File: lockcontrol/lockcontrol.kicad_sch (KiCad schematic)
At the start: 8 parts, among them J1 ButtonHeader, K1 G5Q-1A, U1 WeMos_D1_mini, U3 ULN2003, U4 Barrel_Jack_Switch, U5 Barrel_Jack_Switch

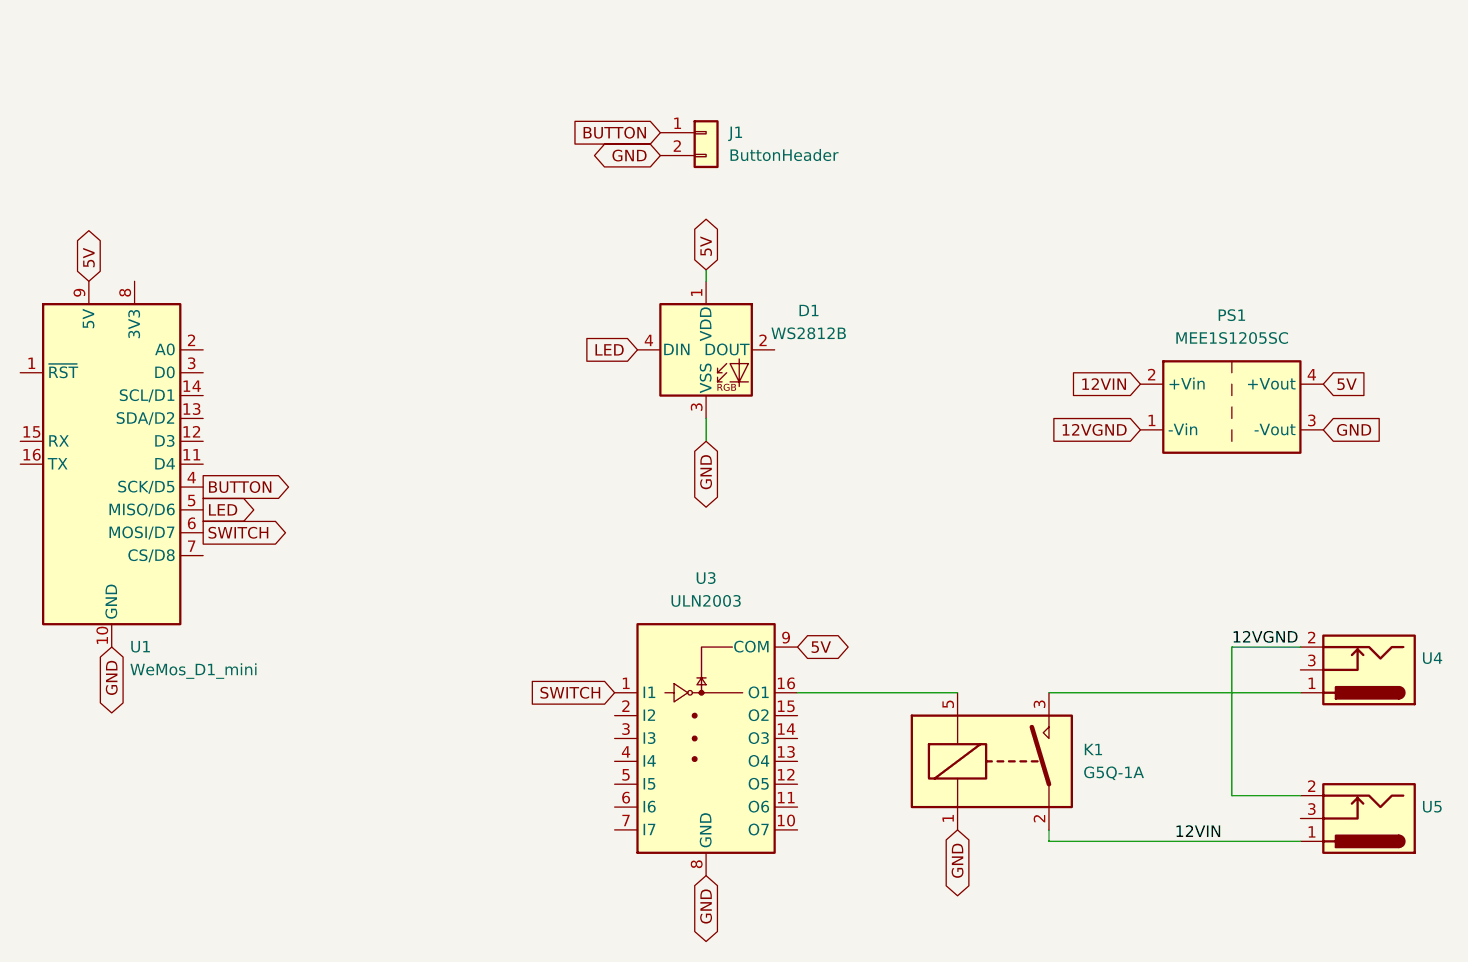
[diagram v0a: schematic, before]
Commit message: update lock control footprints and esp pins
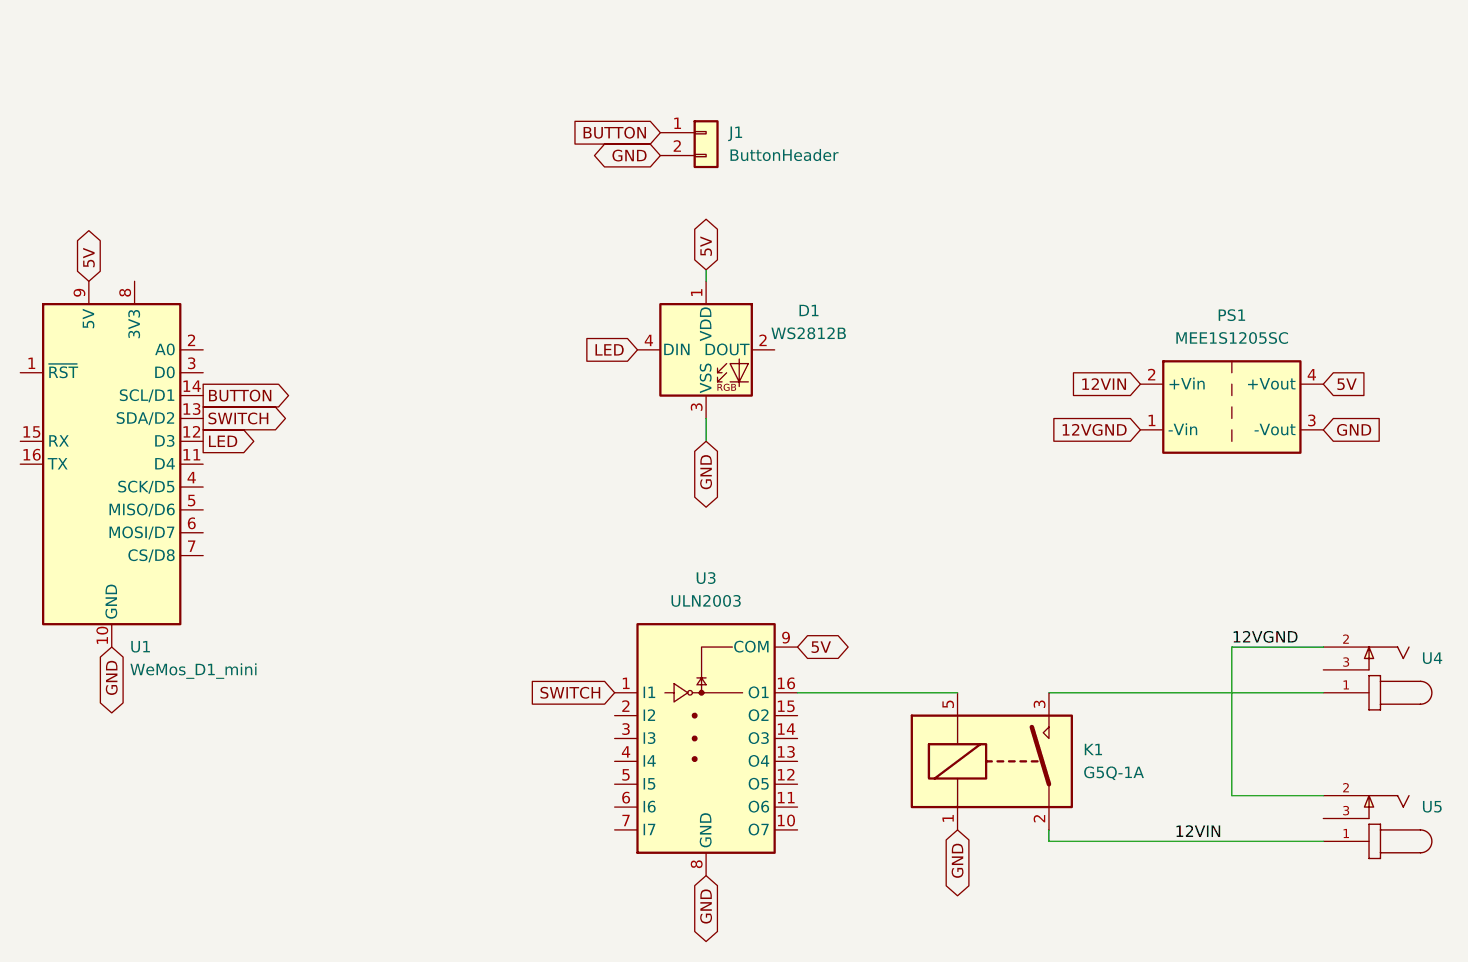
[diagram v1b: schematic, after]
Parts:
- U4, U5: footprint Connector_BarrelJack:BarrelJack_CUI_PJ-102AH_Horizontal -> MyParts:CUI_PJ-002AH; symbol Connector:Barrel_Jack_Switch -> PJ-002AH:PJ-002AH; MANUFACTURER (none) -> CUI INC; STANDARD (none) -> Manufacturer recommendations
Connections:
- net BUTTON: now also U1.14 (SCL/D1); no longer U1.4 (SCK/D5)
- net LED: now also U1.12 (D3); no longer U1.5 (MISO/D6)
- net SWITCH: now also U1.13 (SDA/D2); no longer U1.6 (MOSI/D7)
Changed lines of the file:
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@@
 (kicad_sch (version 20211123) (generator eeschema)
   (paper "A4")
-  (wire (pts (xy 208.28 88.9) (xy 200.66 88.9))
+  (wire (pts (xy 200.66 88.9) (xy 210.82 88.9))
     (stroke (width 0) (type default) (color 0 0 0 0))
   )
@@
     (stroke (width 0) (type default) (color 0 0 0 0))
   )
-  (wire (pts (xy 208.28 110.49) (xy 180.34 110.49))
+  (wire (pts (xy 180.34 110.49) (xy 210.82 110.49))
     (stroke (width 0) (type default) (color 0 0 0 0))
   )
@@
     (stroke (width 0) (type default) (color 0 0 0 0))
   )
-  (wire (pts (xy 180.34 93.98) (xy 208.28 93.98))
-    (stroke (width 0) (type default) (color 0 0 0 0))
-  )
-  (wire (pts (xy 200.66 105.41) (xy 208.28 105.41))
+  (wire (pts (xy 180.34 93.98) (xy 210.82 93.98))
+    (stroke (width 0) (type default) (color 0 0 0 0))
+  )
+  (wire (pts (xy 200.66 105.41) (xy 210.82 105.41))
     (stroke (width 0) (type default) (color 0 0 0 0))
   )
@@
     )
   )
-  (global_label "SWITCH" (shape output) (at 86.36 76.2 0) (fields_autoplaced)
-    (effects (font (size 1.27 1.27)) (justify left))
-    (property "Intersheet References" "${INTERSHEET_REFS}" (id 0) (at 95.6069 76.1206 0)
+  (global_label "SWITCH" (shape output) (at 86.36 63.5 0) (fields_autoplaced)
+    (effects (font (size 1.27 1.27)) (justify left))
+    (property "Intersheet References" "${INTERSHEET_REFS}" (id 0) (at 95.6069 63.4206 0)
       (effects (font (size 1.27 1.27)) (justify left) hide)
     )
@@
     )
   )
-  (global_label "BUTTON" (shape output) (at 86.36 71.12 0) (fields_autoplaced)
-    (effects (font (size 1.27 1.27)) (justify left))
-    (property "Intersheet References" "${INTERSHEET_REFS}" (id 0) (at 95.9698 71.0406 0)
+  (global_label "BUTTON" (shape output) (at 86.36 60.96 0) (fields_autoplaced)
+    (effects (font (size 1.27 1.27)) (justify left))
+    (property "Intersheet References" "${INTERSHEET_REFS}" (id 0) (at 95.9698 60.8806 0)
       (effects (font (size 1.27 1.27)) (justify left) hide)
     )
@@
     )
   )
-  (global_label "LED" (shape output) (at 86.36 73.66 0) (fields_autoplaced)
-    (effects (font (size 1.27 1.27)) (justify left))
-    (property "Intersheet References" "${INTERSHEET_REFS}" (id 0) (at 92.2202 73.5806 0)
+  (global_label "LED" (shape output) (at 86.36 66.04 0) (fields_autoplaced)
+    (effects (font (size 1.27 1.27)) (justify left))
+    (property "Intersheet References" "${INTERSHEET_REFS}" (id 0) (at 92.2202 65.9606 0)
       (effects (font (size 1.27 1.27)) (justify left) hide)
     )
@@
     (pin "9")
   )
-  (symbol (lib_id "Connector:Barrel_Jack_Switch") (at 215.9 107.95 180) (unit 1)
+  (symbol (lib_id "PJ-002AH:PJ-002AH") (at 215.9 107.95 180) (unit 1)
     (in_bom yes) (on_board yes)
     (property "Reference" "U5" (id 0) (at 221.742 106.68 0)
@@
       (effects (font (size 1.27 1.27)) (justify right) hide)
     )
-    (property "Footprint" "Connector_BarrelJack:BarrelJack_CUI_PJ-102AH_Horizontal" (id 2) (at 214.63 106.934 0)
-      (effects (font (size 1.27 1.27)) hide)
-    )
-    (property "Datasheet" "~" (id 3) (at 214.63 106.934 0)
-      (effects (font (size 1.27 1.27)) hide)
-    )
-    (pin "1")
-    (pin "2")
-    (pin "3")
-  )
-  (symbol (lib_id "Connector:Barrel_Jack_Switch") (at 215.9 91.44 180) (unit 1)
+    (property "Footprint" "MyParts:CUI_PJ-002AH" (id 2) (at 215.9 107.95 0)
+      (effects (font (size 1.27 1.27)) (justify left bottom) hide)
+    )
+    (property "Datasheet" "~" (id 3) (at 215.9 107.95 0)
+      (effects (font (size 1.27 1.27)) (justify left bottom) hide)
+    )
+    (property "STANDARD" "Manufacturer recommendations" (id 4) (at 215.9 107.95 0)
+      (effects (font (size 1.27 1.27)) (justify left bottom) hide)
+    )
+    (property "MANUFACTURER" "CUI INC" (id 5) (at 215.9 107.95 0)
+      (effects (font (size 1.27 1.27)) (justify left bottom) hide)
+    )
+    (pin "1")
+    (pin "2")
+    (pin "3")
+  )
+  (symbol (lib_id "PJ-002AH:PJ-002AH") (at 215.9 91.44 180) (unit 1)
     (in_bom yes) (on_board yes)
     (property "Reference" "U4" (id 0) (at 221.742 90.17 0)
@@
       (effects (font (size 1.27 1.27)) (justify right) hide)
     )
-    (property "Footprint" "Connector_BarrelJack:BarrelJack_CUI_PJ-102AH_Horizontal" (id 2) (at 214.63 90.424 0)
-      (effects (font (size 1.27 1.27)) hide)
-    )
-    (property "Datasheet" "~" (id 3) (at 214.63 90.424 0)
-      (effects (font (size 1.27 1.27)) hide)
+    (property "Footprint" "MyParts:CUI_PJ-002AH" (id 2) (at 215.9 91.44 0)
+      (effects (font (size 1.27 1.27)) (justify left bottom) hide)
+    )
+    (property "Datasheet" "~" (id 3) (at 215.9 91.44 0)
+      (effects (font (size 1.27 1.27)) (justify left bottom) hide)
+    )
+    (property "STANDARD" "Manufacturer recommendations" (id 4) (at 215.9 91.44 0)
+      (effects (font (size 1.27 1.27)) (justify left bottom) hide)
+    )
+    (property "MANUFACTURER" "CUI INC" (id 5) (at 215.9 91.44 0)
+      (effects (font (size 1.27 1.27)) (justify left bottom) hide)
     )
     (pin "1")
@@
     )
     (path "/82df6006-3509-4776-a691-c87254d03f97"
-      (reference "U4") (unit 1) (value "Barrel_Jack_Switch") (footprint "Connector_BarrelJack:BarrelJack_CUI_PJ-102AH_Horizontal")
+      (reference "U4") (unit 1) (value "Barrel_Jack_Switch") (footprint "MyParts:CUI_PJ-002AH")
     )
     (path "/6c440d2a-4abb-42b7-834c-5e367a742a46"
-      (reference "U5") (unit 1) (value "Barrel_Jack_Switch") (footprint "Connector_BarrelJack:BarrelJack_CUI_PJ-102AH_Horizontal")
-    )
-  )
+      (reference "U5") (unit 1) (value "Barrel_Jack_Switch") (footprint "MyParts:CUI_PJ-002AH")
+    )
+  )

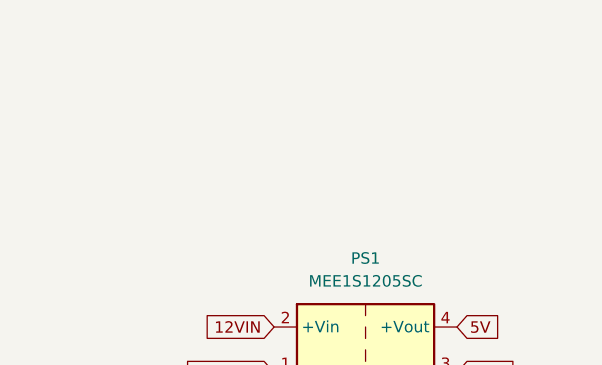
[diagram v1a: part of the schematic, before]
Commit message: add mounting holes
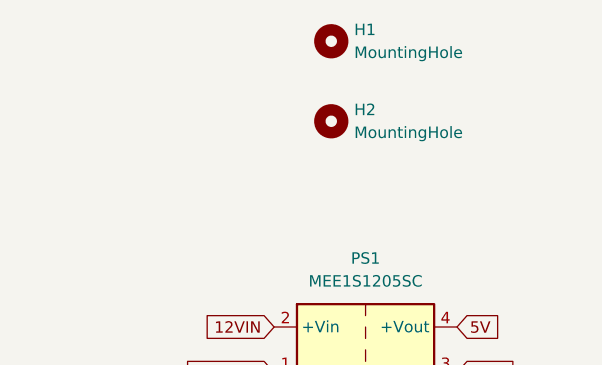
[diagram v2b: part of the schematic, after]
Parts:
- added H1, H2: MountingHole, MountingHole:MountingHole_2.1mm, symbol Mechanical:MountingHole
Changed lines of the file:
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@@
     (pin "2")
+  )
+  (symbol (lib_id "Mechanical:MountingHole") (at 196.85 27.94 0) (unit 1)
+    (in_bom yes) (on_board yes) (fields_autoplaced)
+    (property "Reference" "H1" (id 0) (at 199.39 26.6699 0)
+      (effects (font (size 1.27 1.27)) (justify left))
+    )
+    (property "Value" "MountingHole" (id 1) (at 199.39 29.2099 0)
+      (effects (font (size 1.27 1.27)) (justify left))
+    )
+    (property "Footprint" "MountingHole:MountingHole_2.1mm" (id 2) (at 196.85 27.94 0)
+      (effects (font (size 1.27 1.27)) hide)
+    )
+    (property "Datasheet" "~" (id 3) (at 196.85 27.94 0)
+      (effects (font (size 1.27 1.27)) hide)
+    )
+  )
+  (symbol (lib_id "Mechanical:MountingHole") (at 196.85 36.83 0) (unit 1)
+    (in_bom yes) (on_board yes) (fields_autoplaced)
+    (property "Reference" "H2" (id 0) (at 199.39 35.5599 0)
+      (effects (font (size 1.27 1.27)) (justify left))
+    )
+    (property "Value" "MountingHole" (id 1) (at 199.39 38.0999 0)
+      (effects (font (size 1.27 1.27)) (justify left))
+    )
+    (property "Footprint" "MountingHole:MountingHole_2.1mm" (id 2) (at 196.85 36.83 0)
+      (effects (font (size 1.27 1.27)) hide)
+    )
+    (property "Datasheet" "~" (id 3) (at 196.85 36.83 0)
+      (effects (font (size 1.27 1.27)) hide)
+    )
   )
   (sheet_instances
@@
       (reference "D1") (unit 1) (value "WS2812B") (footprint "LED_SMD:LED_WS2812B_PLCC4_5.0x5.0mm_P3.2mm")
     )
+    (path "/e558ff88-3d2d-466f-a272-347b78565264"
+      (reference "H1") (unit 1) (value "MountingHole") (footprint "MountingHole:MountingHole_2.1mm")
+    )
+    (path "/f9b7baa8-7583-43cb-9e86-8d81cb49946e"
+      (reference "H2") (unit 1) (value "MountingHole") (footprint "MountingHole:MountingHole_2.1mm")
+    )
     (path "/c956d2ad-dbd9-4e00-9b84-0722181e4fec"

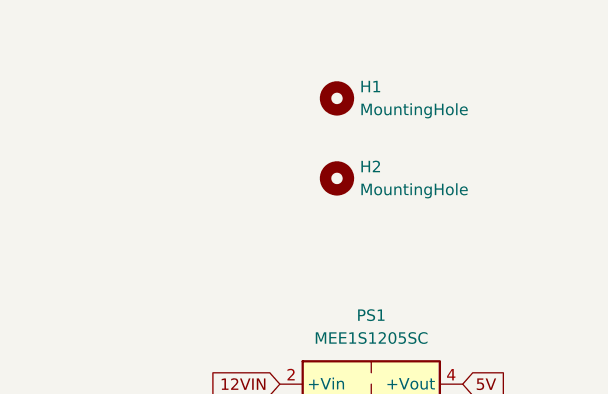
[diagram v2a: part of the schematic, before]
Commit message: mounting holes
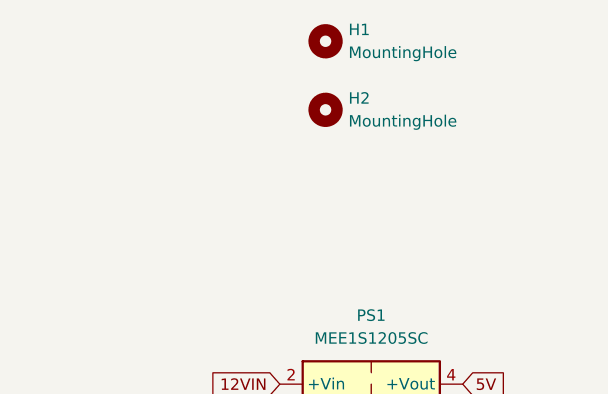
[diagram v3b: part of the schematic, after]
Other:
- moved on the sheet: H1, H2
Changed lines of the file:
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@@
     (pin "2")
   )
-  (symbol (lib_id "Mechanical:MountingHole") (at 196.85 27.94 0) (unit 1)
+  (symbol (lib_id "Mechanical:MountingHole") (at 195.58 21.59 0) (unit 1)
     (in_bom yes) (on_board yes) (fields_autoplaced)
-    (property "Reference" "H1" (id 0) (at 199.39 26.6699 0)
+    (property "Reference" "H1" (id 0) (at 198.12 20.3199 0)
       (effects (font (size 1.27 1.27)) (justify left))
     )
-    (property "Value" "MountingHole" (id 1) (at 199.39 29.2099 0)
+    (property "Value" "MountingHole" (id 1) (at 198.12 22.8599 0)
       (effects (font (size 1.27 1.27)) (justify left))
     )
-    (property "Footprint" "MountingHole:MountingHole_2.1mm" (id 2) (at 196.85 27.94 0)
+    (property "Footprint" "MountingHole:MountingHole_2.1mm" (id 2) (at 195.58 21.59 0)
       (effects (font (size 1.27 1.27)) hide)
     )
-    (property "Datasheet" "~" (id 3) (at 196.85 27.94 0)
+    (property "Datasheet" "~" (id 3) (at 195.58 21.59 0)
       (effects (font (size 1.27 1.27)) hide)
     )
   )
-  (symbol (lib_id "Mechanical:MountingHole") (at 196.85 36.83 0) (unit 1)
+  (symbol (lib_id "Mechanical:MountingHole") (at 195.58 29.21 0) (unit 1)
     (in_bom yes) (on_board yes) (fields_autoplaced)
-    (property "Reference" "H2" (id 0) (at 199.39 35.5599 0)
+    (property "Reference" "H2" (id 0) (at 198.12 27.9399 0)
       (effects (font (size 1.27 1.27)) (justify left))
     )
-    (property "Value" "MountingHole" (id 1) (at 199.39 38.0999 0)
+    (property "Value" "MountingHole" (id 1) (at 198.12 30.4799 0)
       (effects (font (size 1.27 1.27)) (justify left))
     )
-    (property "Footprint" "MountingHole:MountingHole_2.1mm" (id 2) (at 196.85 36.83 0)
+    (property "Footprint" "MountingHole:MountingHole_2.1mm" (id 2) (at 195.58 29.21 0)
       (effects (font (size 1.27 1.27)) hide)
     )
-    (property "Datasheet" "~" (id 3) (at 196.85 36.83 0)
+    (property "Datasheet" "~" (id 3) (at 195.58 29.21 0)
       (effects (font (size 1.27 1.27)) hide)
     )

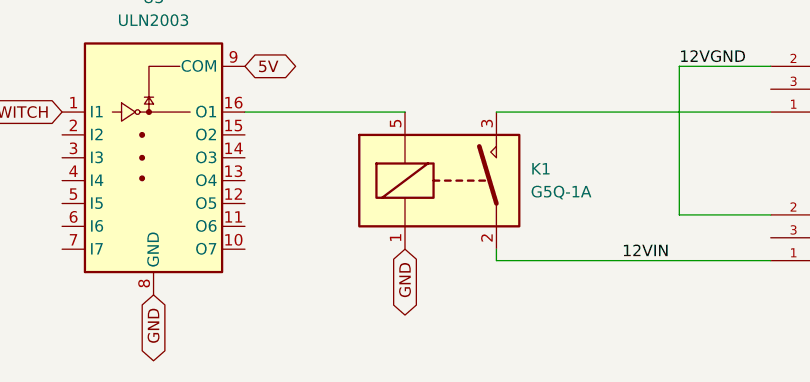
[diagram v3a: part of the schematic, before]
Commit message: relay driver is grounding, pass 5V through relay then
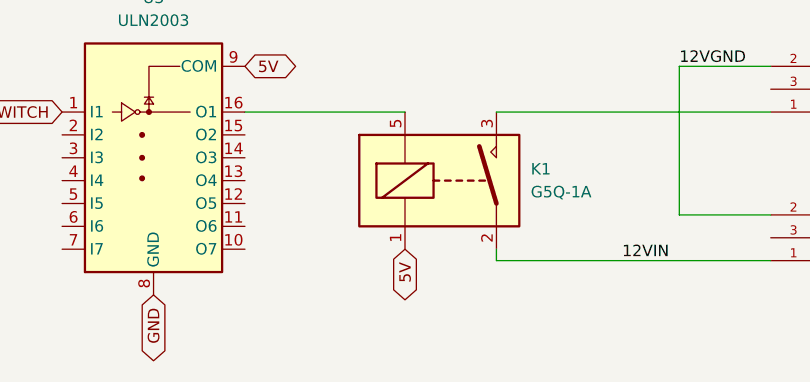
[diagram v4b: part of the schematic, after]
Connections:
- net 5V: now also K1.1
- net GND: no longer K1.1
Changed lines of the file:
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@@
     )
   )
-  (global_label "GND" (shape bidirectional) (at 170.18 109.22 270) (fields_autoplaced)
+  (global_label "5V" (shape bidirectional) (at 170.18 109.22 270) (fields_autoplaced)
     (effects (font (size 1.27 1.27)) (justify right))
-    (property "Intersheet References" "${INTERSHEET_REFS}" (id 0) (at 170.2594 115.5036 90)
+    (property "Intersheet References" "${INTERSHEET_REFS}" (id 0) (at 170.1006 113.9312 90)
       (effects (font (size 1.27 1.27)) (justify right) hide)
     )

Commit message: capture before removing disk
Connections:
- net LED: now also U1.7 (CS/D8); no longer U1.12 (D3)
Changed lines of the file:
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@@
     )
   )
-  (global_label "LED" (shape output) (at 86.36 66.04 0) (fields_autoplaced)
+  (global_label "LED" (shape output) (at 86.36 78.74 0) (fields_autoplaced)
     (effects (font (size 1.27 1.27)) (justify left))
-    (property "Intersheet References" "${INTERSHEET_REFS}" (id 0) (at 92.2202 65.9606 0)
+    (property "Intersheet References" "${INTERSHEET_REFS}" (id 0) (at 92.2202 78.6606 0)
       (effects (font (size 1.27 1.27)) (justify left) hide)
     )
